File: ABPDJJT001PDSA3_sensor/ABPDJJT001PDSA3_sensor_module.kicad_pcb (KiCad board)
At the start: 4 copper layers, 29 x 29.5 mm, 4 parts, among them J1 Conn_02x04_Odd_Even, J2 Conn_02x07_Odd_Even, U1 ABPDJJ001PDSA3

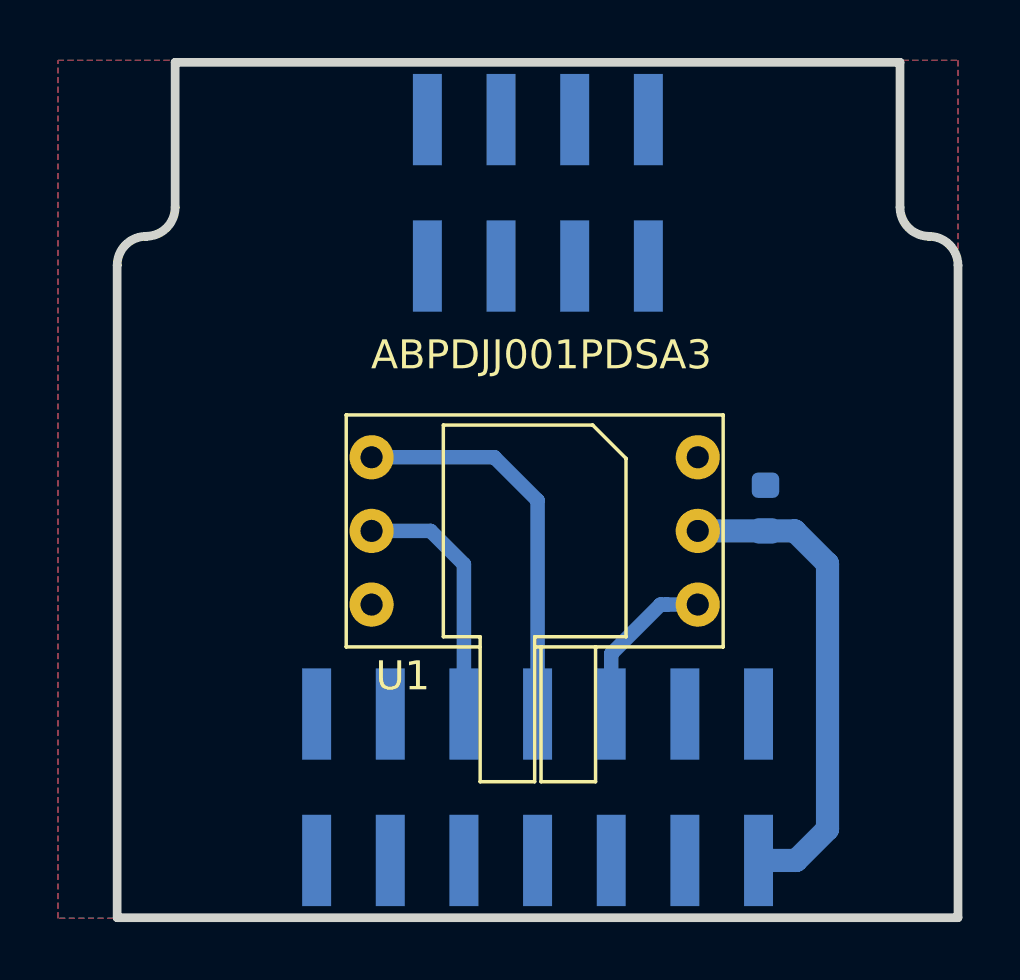
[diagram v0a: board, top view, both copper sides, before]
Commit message: J2 connector modified
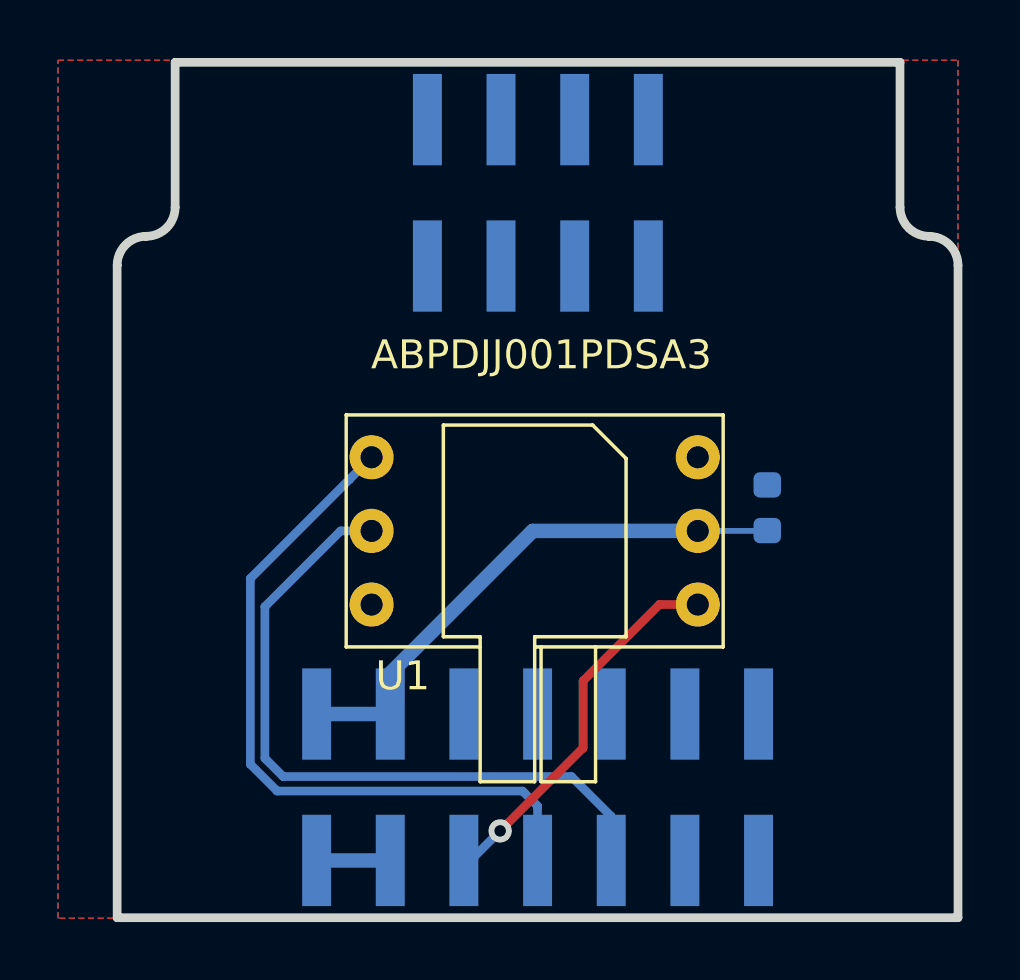
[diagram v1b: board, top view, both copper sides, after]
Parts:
- moved C1 0.06 mm to (120.9, 45.4)
- turned J2 to 270 degrees
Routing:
- net /SPI_MISO: track 8.83 -> 24.3 mm
- net /SPI_CLK: track 13.7 -> 24.7 mm
- net /SPI_CS: track 6.97 -> 13.2 mm, vias 0 -> 1
- net +5V: track 0.00 -> 2.54 mm
- net +3V3: track 16.9 -> 19.0 mm
- net /Analog: track 0.00 -> 1.20 mm
